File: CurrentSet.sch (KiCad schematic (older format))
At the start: 7 parts, among them Q15 MMBT3904, U10 LM358

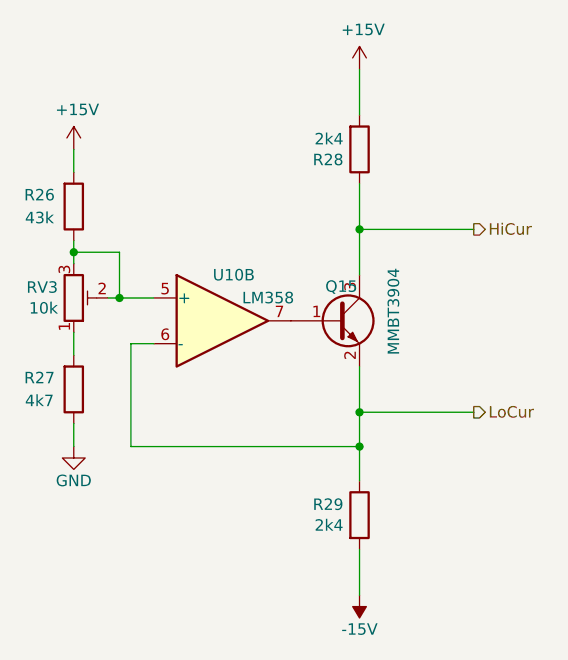
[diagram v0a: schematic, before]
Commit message: Fixed some bugs, finished block symbols
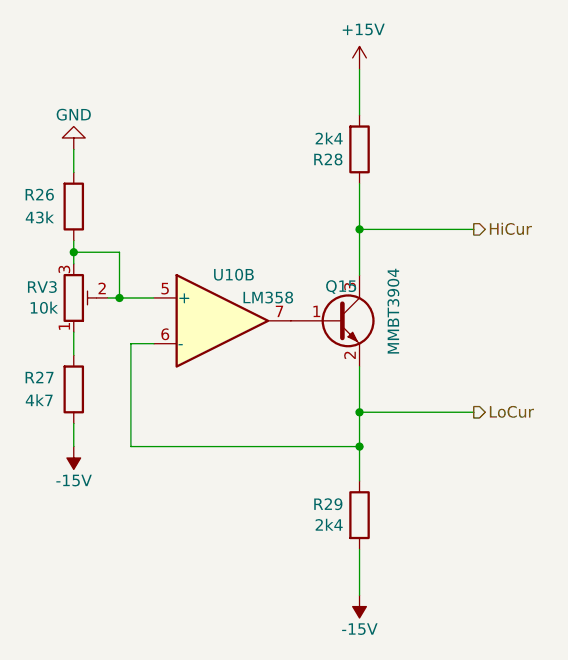
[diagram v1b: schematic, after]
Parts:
- RV3: footprint Potentiometer_THT:Potentiometer_Bourns_3299W_Vertical -> Potentiometer_THT:Potentiometer_Bourns_3296W_Vertical
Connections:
- net +15V: no longer R26.2
- net -15V: now also R27.1
- net GND: now also R26.2; no longer R27.1
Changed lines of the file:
@@
 encoding utf-8
 Sheet 9 13
-Title ""
-Date ""
-Rev ""
-Comp ""
+Title "Size Adjustment"
+Date "2021-04-20"
+Rev "2.0"
+Comp "Filip Piórski"
 Comment1 ""
 Comment2 ""
@@
 F 0 "RV3" H 3581 5054 50  0000 R CNN
 F 1 "10k" H 3581 5145 50  0000 R CNN
-F 2 "Potentiometer_THT:Potentiometer_Bourns_3299W_Vertical" H 3650 5100 50  0001 C CNN
+F 2 "Potentiometer_THT:Potentiometer_Bourns_3296W_Vertical" H 3650 5100 50  0001 C CNN
 F 3 "~" H 3650 5100 50  0001 C CNN
 	1    3650 5100
@@
 L power:GND #PWR?
 U 1 1 6044B532
-P 3650 5750
+P 3650 4450
 AR Path="/5FA4B51C/6044B532" Ref="#PWR?"  Part="1"
 AR Path="/601DE80D/6044B532" Ref="#PWR?"  Part="1"
@@
 AR Path="/601DE80D/604476D8/6044B532" Ref="#PWR?"  Part="1"
 AR Path="/601E8CDA/6044B532" Ref="#PWR087"  Part="1"
-F 0 "#PWR087" H 3650 5500 50  0001 C CNN
-F 1 "GND" H 3650 5600 50  0000 C CNN
-F 2 "" H 3650 5750 50  0001 C CNN
-F 3 "" H 3650 5750 50  0001 C CNN
-	1    3650 5750
-	1    0    0    -1
-$EndComp
-$Comp
-L power:+15V #PWR?
-U 1 1 6044B538
-P 3650 4450
-AR Path="/5FA4B51C/6044B538" Ref="#PWR?"  Part="1"
-AR Path="/601DE80D/6044B538" Ref="#PWR?"  Part="1"
-AR Path="/6044B538" Ref="#PWR?"  Part="1"
-AR Path="/604476D8/6044B538" Ref="#PWR?"  Part="1"
-AR Path="/601DE80D/604476D8/6044B538" Ref="#PWR?"  Part="1"
-AR Path="/601E8CDA/6044B538" Ref="#PWR086"  Part="1"
-F 0 "#PWR086" H 3650 4300 50  0001 C CNN
-F 1 "+15V" H 3665 4623 50  0000 C CNN
+F 0 "#PWR087" H 3650 4200 50  0001 C CNN
+F 1 "GND" H 3650 4300 50  0000 C CNN
 F 2 "" H 3650 4450 50  0001 C CNN
 F 3 "" H 3650 4450 50  0001 C CNN
 	1    3650 4450
-	1    0    0    -1
+	-1   0    0    1
 $EndComp
 $Comp
@@
 Text HLabel 5400 5600 2    50   Output ~ 0
 LoCur
+$Comp
+L power:-15V #PWR?
+U 1 1 6080B453
+P 3650 5750
+AR Path="/5FA4B51C/6080B453" Ref="#PWR?"  Part="1"
+AR Path="/601DE80D/6080B453" Ref="#PWR?"  Part="1"
+AR Path="/6080B453" Ref="#PWR?"  Part="1"
+AR Path="/604476D8/6080B453" Ref="#PWR?"  Part="1"
+AR Path="/601DE80D/604476D8/6080B453" Ref="#PWR?"  Part="1"
+AR Path="/601E8CDA/6080B453" Ref="#PWR0119"  Part="1"
+F 0 "#PWR0119" H 3650 5850 50  0001 C CNN
+F 1 "-15V" H 3650 5900 50  0000 C CNN
+F 2 "" H 3650 5750 50  0001 C CNN
+F 3 "" H 3650 5750 50  0001 C CNN
+	1    3650 5750
+	1    0    0    1
+$EndComp
 $EndSCHEMATC
